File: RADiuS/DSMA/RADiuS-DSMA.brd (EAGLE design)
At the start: 19.7 x 51.3 mm, 14 parts

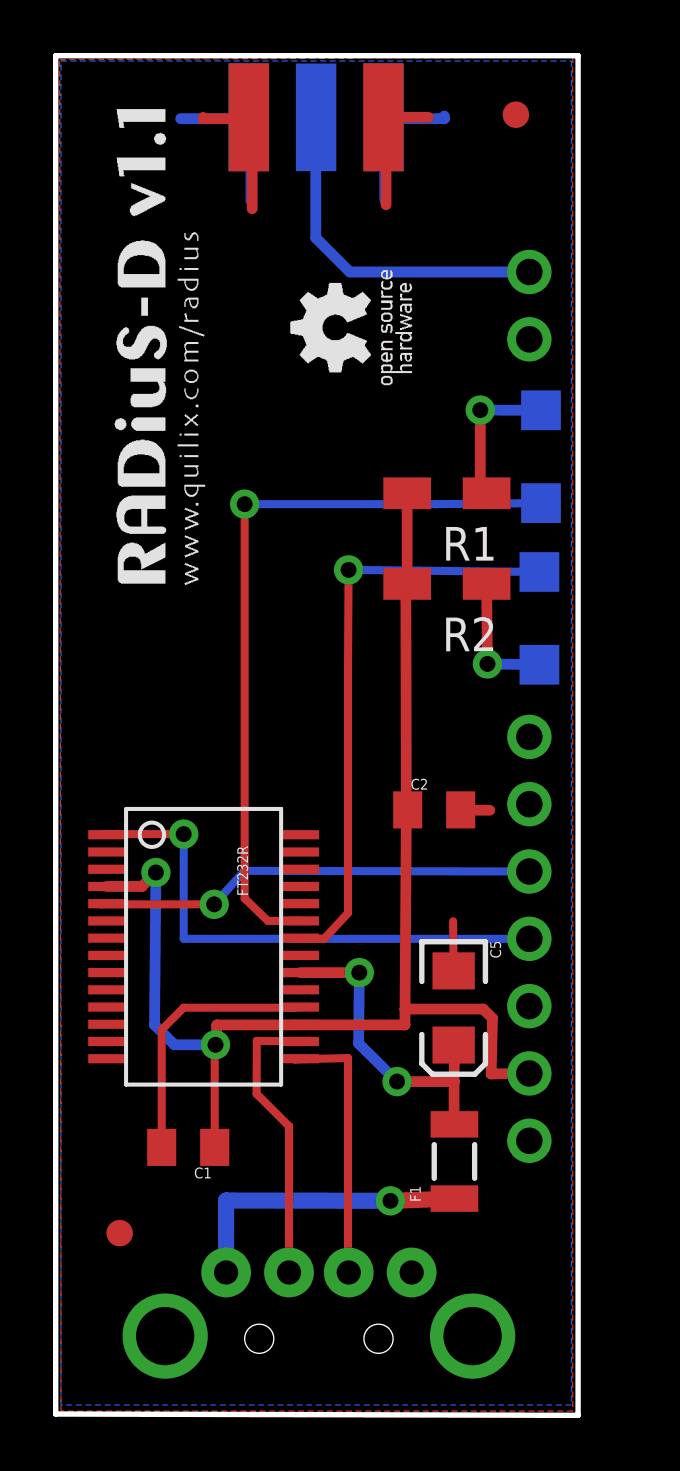
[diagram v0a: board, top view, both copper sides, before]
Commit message: changes to simplify manufacturing + mill-max connectors for radio
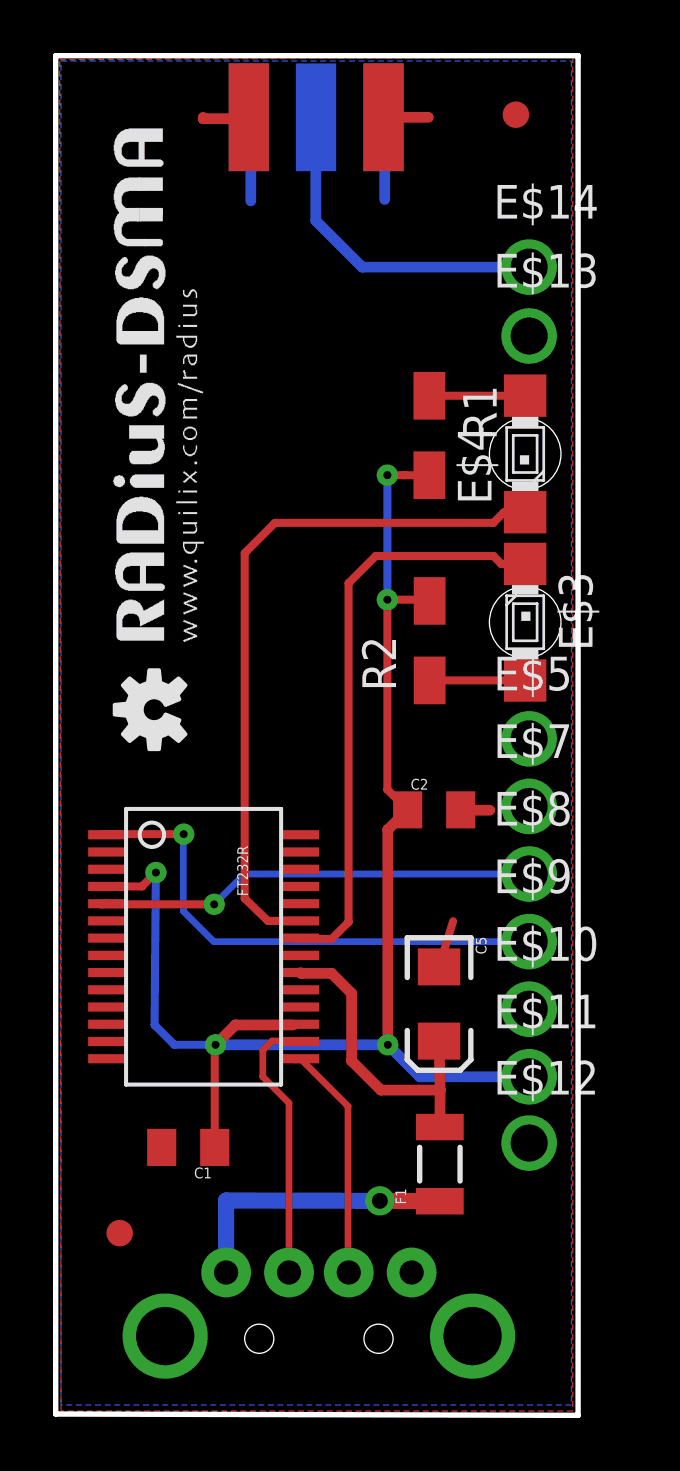
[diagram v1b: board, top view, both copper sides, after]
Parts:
- removed ERA*TRS: (no value), lprs:SIL9
- removed LED1: Red, led:SML1206
- removed LED2: Green, led:SML1206
- added E$10, E$11, E$12, E$13, E$14, E$5, E$7, E$8, E$9: (no value), adafruit_4u:1X01-CLEANBIG
- added E$3, E$4: (no value), led:MINI-TOPLED-SANTANA
- added E$6: (no value), SparkFun:OSHW-LOGO-S
- moved R1 2.28 mm to (15.3, 37.9), turned to 270 degrees
- moved R2 2.24 mm to (15.3, 30.2), turned to 90 degrees
- moved C5 0.57 mm to (15.7, 16.4)
- moved F1 0.56 mm to (15.7, 10.4)
- renumbered E$2 to E$15
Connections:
- net 3.3V: now also E$11.1; no longer ERA*TRS.8
- net ANT: now also E$14.1; no longer ERA*TRS.1
- net GND: now also E$10.1, E$12.1, E$13.1, GND.GND@0, GND.GND@1; no longer ERA*TRS.2, ERA*TRS.7, ERA*TRS.9
- net N$1: now also E$4.A; no longer LED1.A
- net N$2: now also E$3.A; no longer LED2.A
- net RXD: now also E$8.1; no longer ERA*TRS.5
- net RXLED: now also E$3.C; no longer LED2.C
- net TXD: now also E$9.1; no longer ERA*TRS.6
- net TXLED: now also E$4.C; no longer LED1.C
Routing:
- net GND: track 30.0 -> 10.6 mm
- net 3.3V: track 50.0 -> 55.7 mm, vias 2 -> 5
- net N$1: track 5.60 -> 3.62 mm, vias 1 -> 0
- net TXLED: track 28.5 -> 26.7 mm, vias 1 -> 0
- net N$2: track 4.98 -> 3.61 mm, vias 1 -> 0
- net USB_D+: track 10.3 -> 9.05 mm
- net TXD: track 20.2 -> 19.7 mm
- net N$3: track 11.3 -> 10.8 mm
- net USB_D-: track 10.9 -> 10.4 mm
- net RXLED: track 22.8 -> 22.3 mm, vias 1 -> 0
- net S$2: track 12.2 -> 12.5 mm, vias 2 -> 0

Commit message: update to Eagle 7.7.0
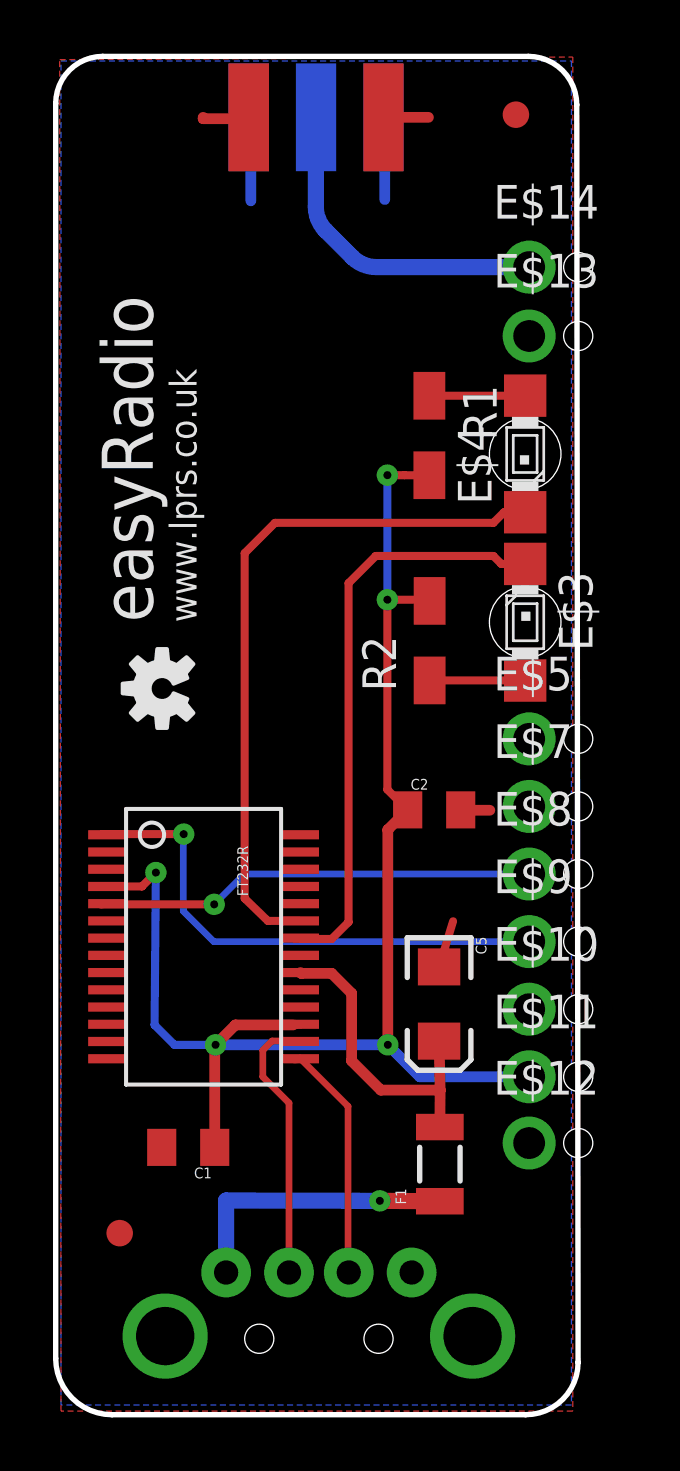
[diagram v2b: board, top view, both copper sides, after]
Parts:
- moved E$6 0.85 mm to (5.25, 28.4)
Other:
- board size 19.7 x 51.3 mm -> 19.7 x 51.2 mm
- board text added: "easyRadio"
- board text added: "www.lprs.co.uk"
